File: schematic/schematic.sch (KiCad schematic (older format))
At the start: 19 parts, among them J1 Conn_Arduino, J2 Conn_Arduino, J3 Conn_Arduino, J4 Conn_Arduino

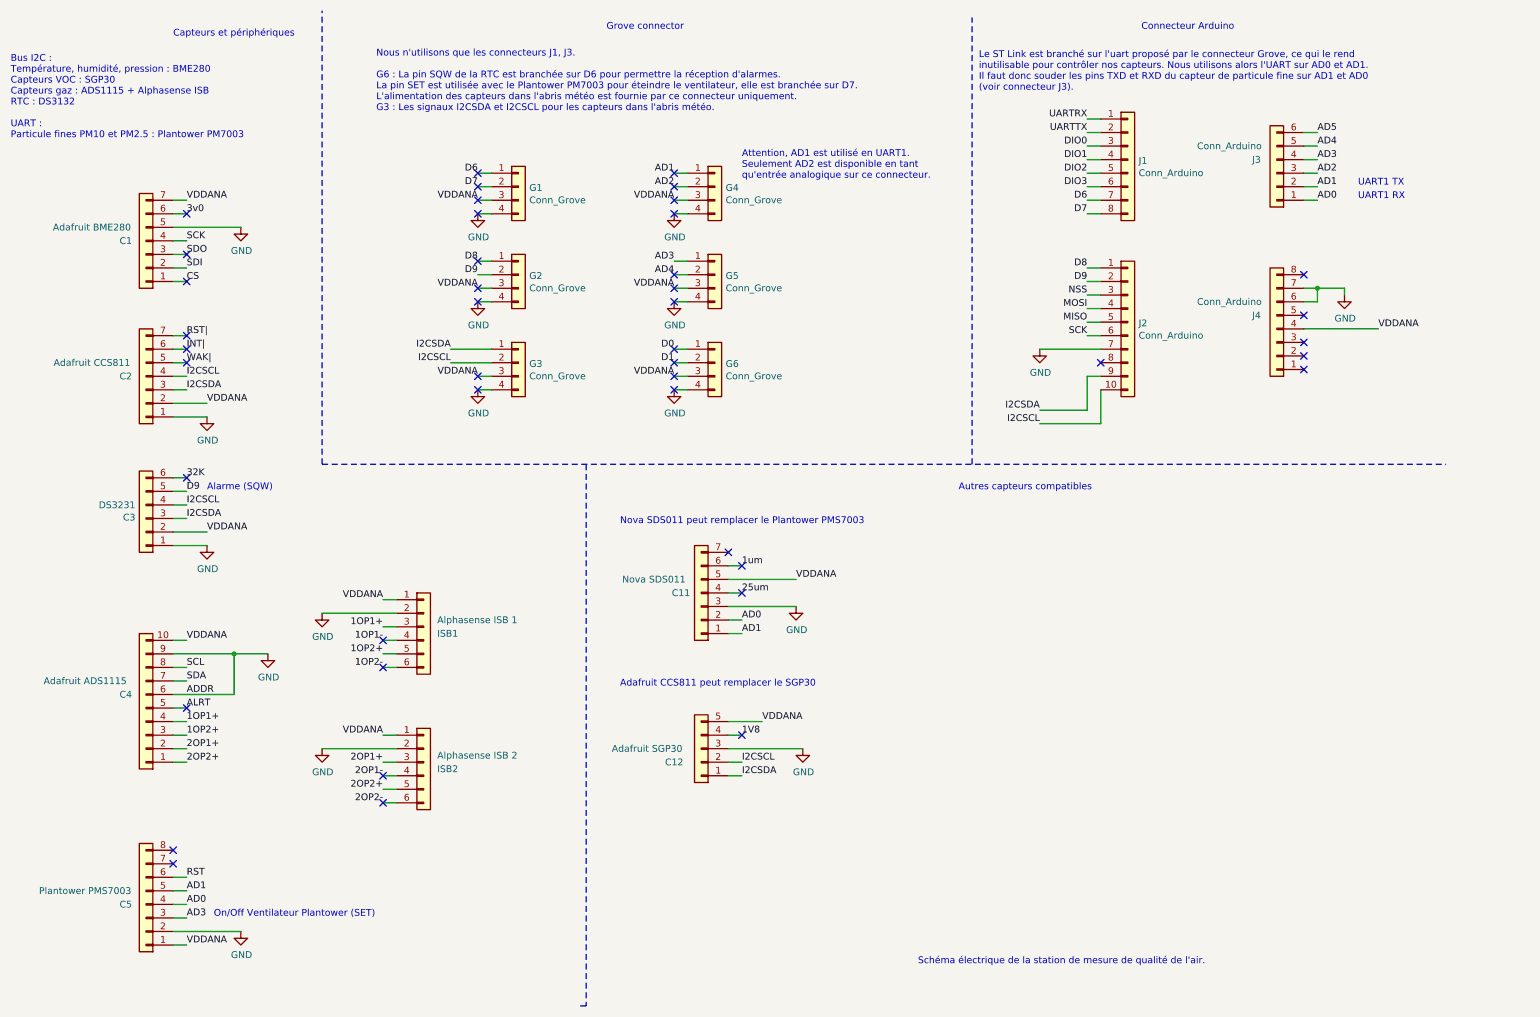
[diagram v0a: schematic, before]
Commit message: change pins on grove connectors
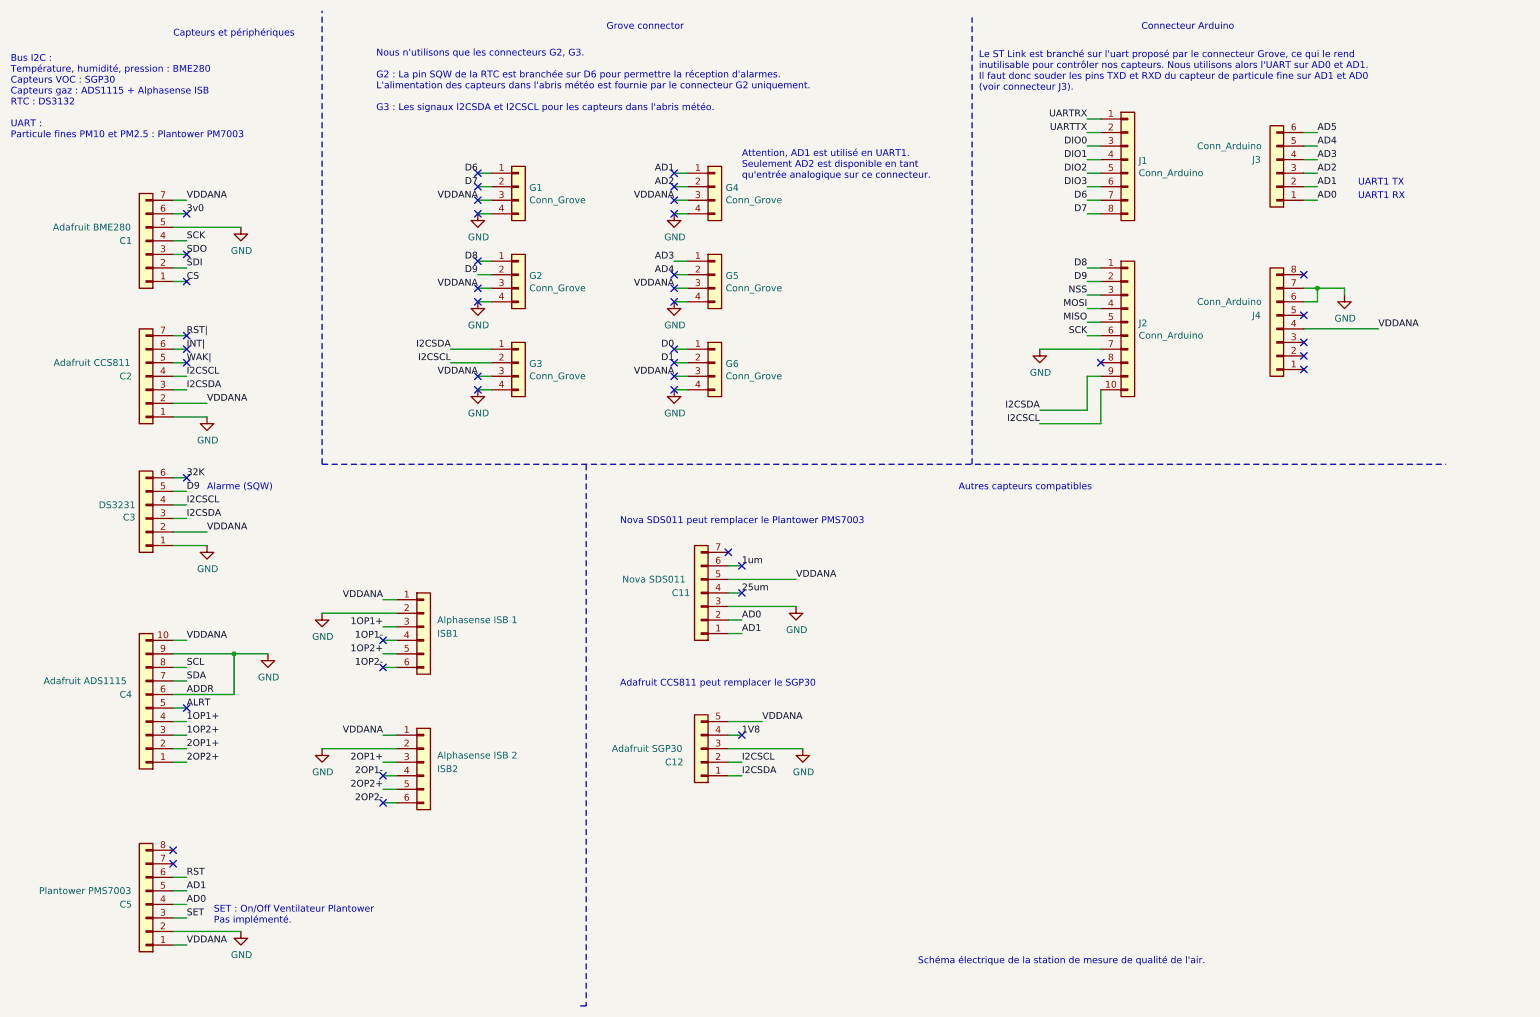
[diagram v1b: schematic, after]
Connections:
- net AD3: no longer C5.3 (Pin_3)
- new net SET: C5.3 (Pin_3)
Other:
- note added: "Nous n'utilisons que les connecteurs G2, G3.\n\nG2 : La pin SQW de la RTC est branchée sur D6 pour permettre la réception d'alarmes. \nL'alimentation des capteurs dans l'abris météo est fournie par le connecteur G2 uniquement. \n\nG3 : Les signaux I2CSDA et I2CSCL pour les capteurs dans l'abris météo."
- note added: "SET : On/Off Ventilateur Plantower\nPas implémenté."
- note removed: "Nous n'utilisons que les connecteurs J1, J3.\n\nG6 : La pin SQW de la RTC est branchée sur D6 pour permettre la réception d'alarmes. \nLa pin SET est utilisée avec le Plantower PM7003 pour éteindre le ventilateur, elle est branchée sur D7. \nL'alimentation des capteurs dans l'abris météo est fournie par ce connecteur uniquement. \nG3 : Les signaux I2CSDA et I2CSCL pour les capteurs dans l'abris m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"
- note removed: "On/Off Ventilateur Plantower (SET)"
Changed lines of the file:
@@
 AD0
 Text Label 1950 7150 0    50   ~ 0
-AD3
+SET
 Text Label 1950 7350 0    50   ~ 0
 VDDANA
@@
 NoConn ~ 4100 2300
 Text Notes 3350 1200 0    50   ~ 0
-Nous n'utilisons que les connecteurs J1, J3.\n\nG6 : La pin SQW de la RTC est branchée sur D6 pour permettre la réception d'alarmes. \nLa pin SET est utilisée avec le Plantower PM7003 pour éteindre le ventilateur, elle est branchée sur D7. \nL'alimentation des capteurs dans l'abris météo est fournie par ce connecteur uniquement. \nG3 : Les signaux I2CSDA et I2CSCL pour les capteurs dans l'abris météo.
+Nous n'utilisons que les connecteurs G2, G3.\n\nG2 : La pin SQW de la RTC est branchée sur D6 pour permettre la réception d'alarmes. \nL'alimentation des capteurs dans l'abris météo est fournie par le connecteur G2 uniquement. \n\nG3 : Les signaux I2CSDA et I2CSCL pour les capteurs dans l'abris météo.
 NoConn ~ 5550 1650
 NoConn ~ 5550 1850
@@
 Text Notes 2100 4000 0    50   ~ 0
 Alarme (SQW)
-Text Notes 2150 7150 0    50   ~ 0
-On/Off Ventilateur Plantower (SET)
+Text Notes 2150 7200 0    50   ~ 0
+SET : On/Off Ventilateur Plantower\nPas implémenté.
 $EndSCHEMATC
